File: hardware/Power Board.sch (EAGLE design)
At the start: 11 parts, among them J1 USB-MICRO-B, U1 MAX1555, U2 MCP1603T-330I/OS, X1 Battery 150mAh, X2 Output

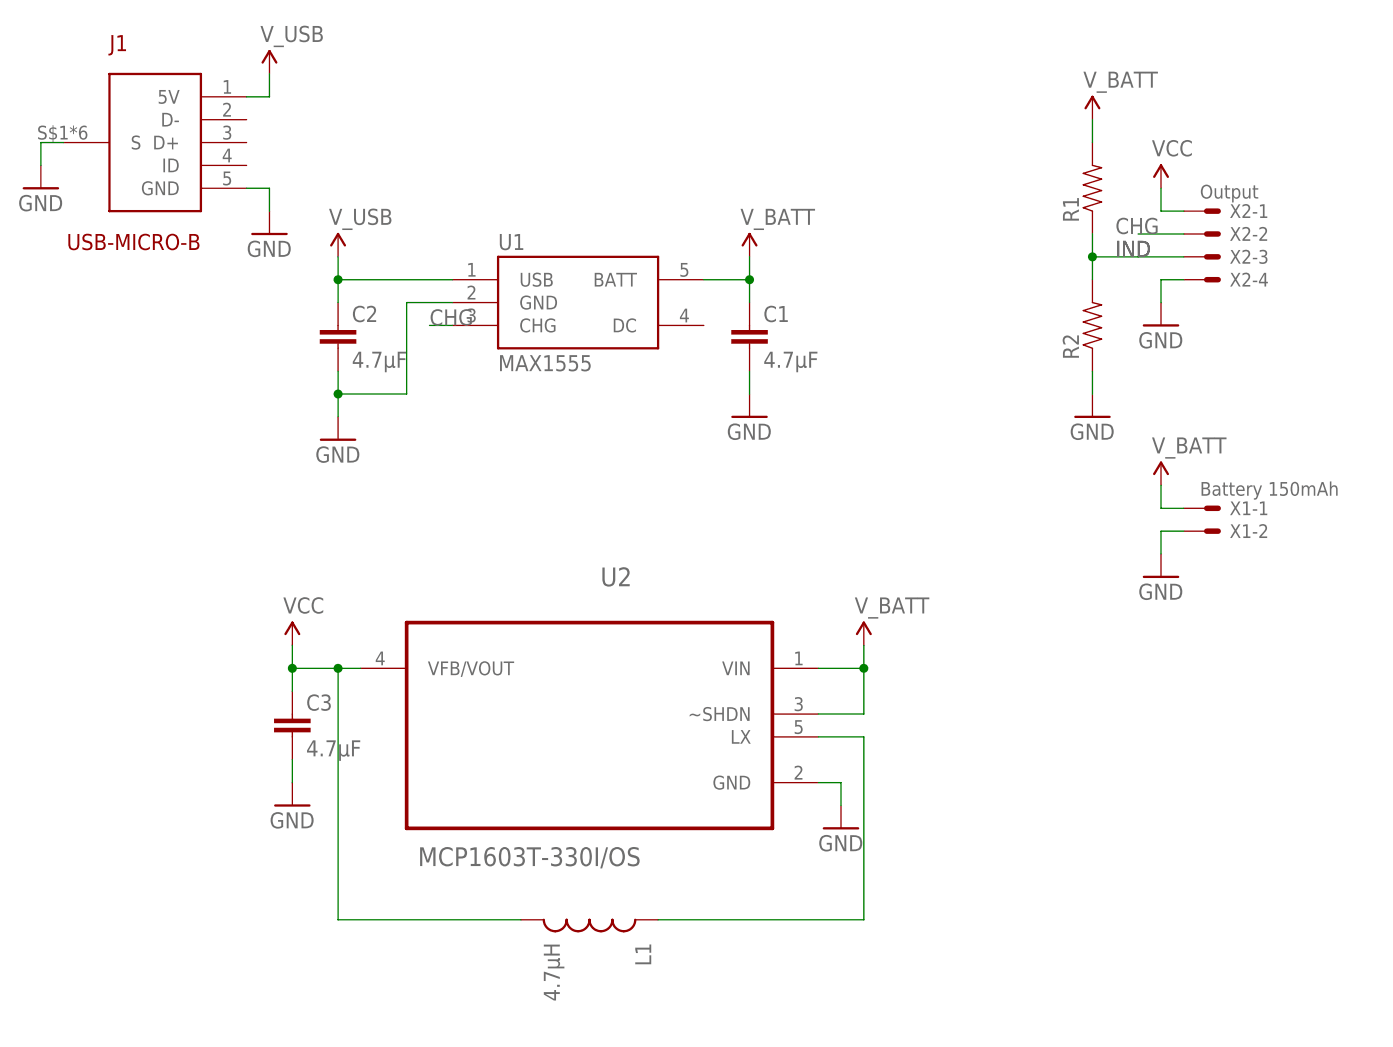
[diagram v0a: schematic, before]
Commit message: Add bitmaps and python code to turn them into valid C++
This python is an abomination 🙃🐍
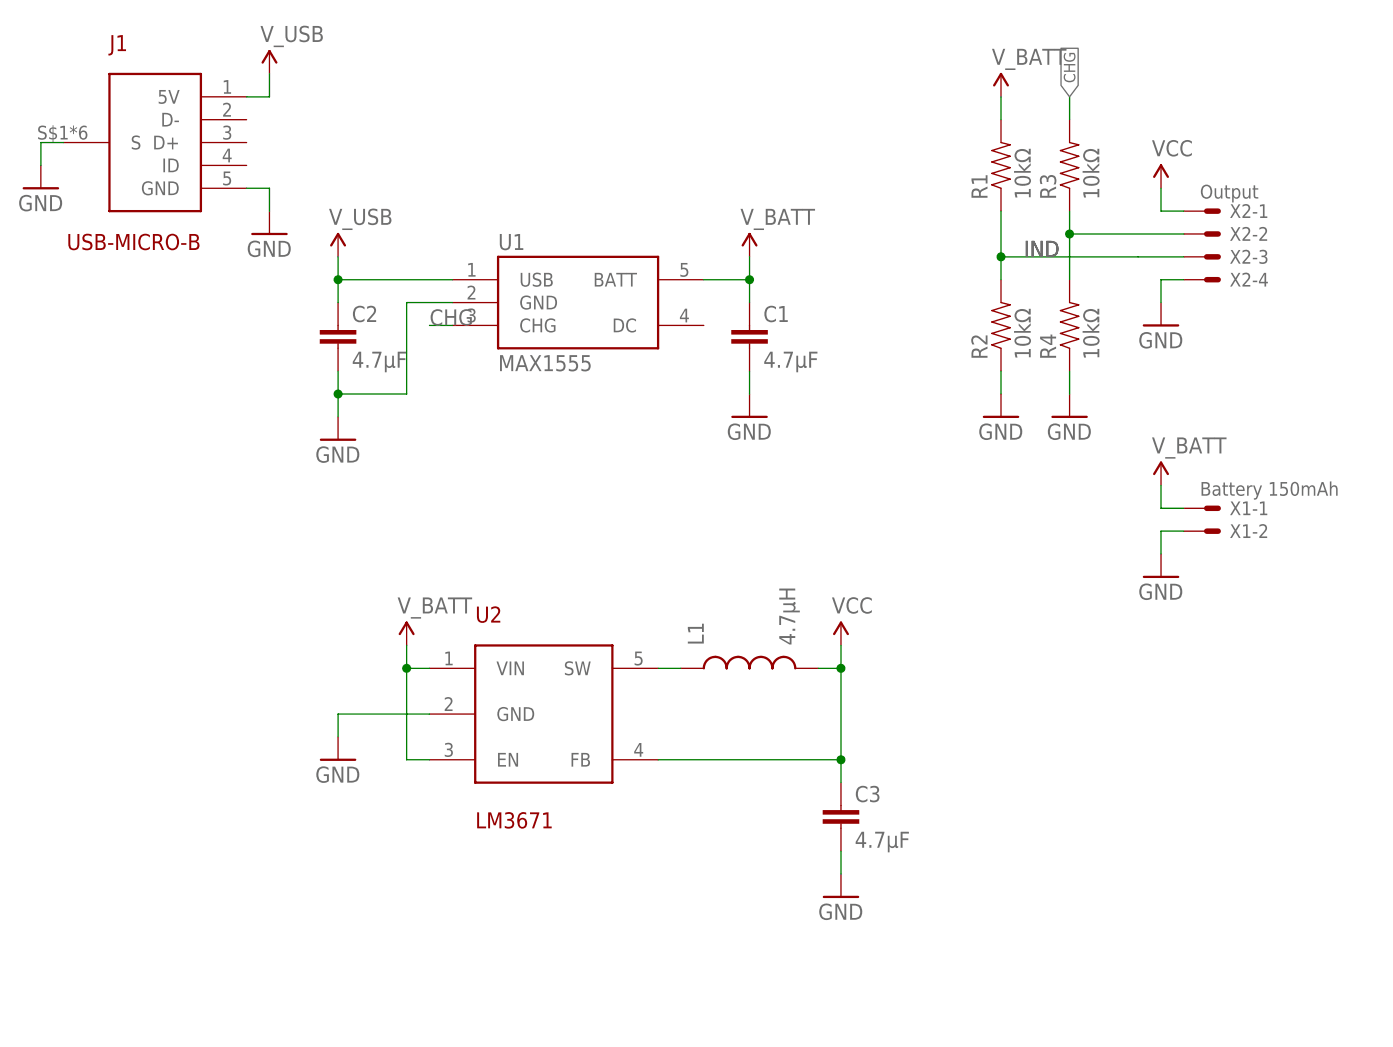
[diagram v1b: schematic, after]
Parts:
- added R3, R4: 10kΩ, SparkFun-Passives:RESISTOR0805-RES
- R1, R2: value (none) -> 10kΩ
- U2: value MCP1603T-330I/OS -> LM3671; device Microchip_By_element14_Batch_1:MCP1603T-330I/OS -> texas-custom:LM3671
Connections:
- removed net N$2: L1.1, U2.LX
- new net CHG_2: R3.1, R4.2, X2-2.S
- new net N$1: L1.1, U2.SW
- net CHG: now also R3.2; no longer X2-2.S
- net GND: now also R4.1
- net VCC: now also U2.FB; no longer U2.VFB/VOUT
- net V_BATT: now also U2.EN; no longer U2.~SHDN
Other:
- moved on the sheet: C3, L1, R1, R2
